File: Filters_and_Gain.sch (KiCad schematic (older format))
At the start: 20 parts, among them U4 OPA388, U5 OPA388, U6 OPA388

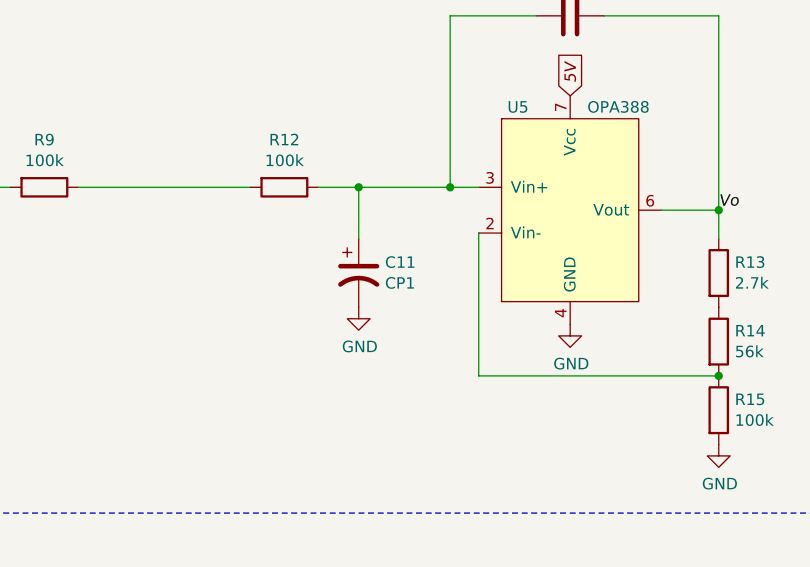
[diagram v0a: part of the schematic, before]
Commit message: Assigned footprints
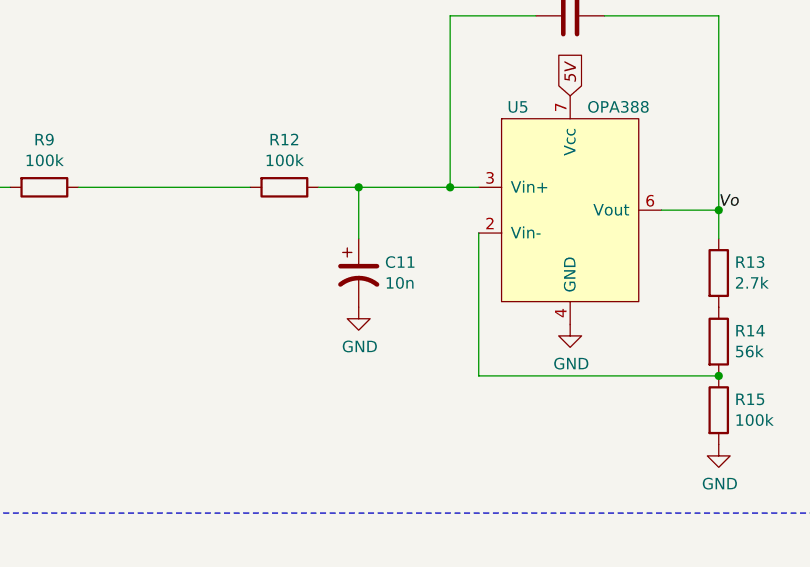
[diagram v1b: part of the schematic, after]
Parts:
- C10, C12, C8, C9: footprint (none) -> Capacitor_SMD:C_0805_2012Metric_Pad1.15x1.40mm_HandSolder
- C11: value CP1 -> 10n; footprint (none) -> Capacitor_SMD:C_0805_2012Metric_Pad1.15x1.40mm_HandSolder
- C13: footprint (none) -> Capacitor_SMD:CP_Elec_6.3x3
- R10, R11, R12, R13, R14, R15, R16, R17, R18, R8, R9: footprint (none) -> Resistor_SMD:R_0805_2012Metric_Pad1.15x1.40mm_HandSolder
- U4, U5, U6: footprint (none) -> Package_SO:SOIC-8_3.9x4.9mm_P1.27mm
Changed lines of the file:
@@
 F 0 "R9" V 2468 2200 50  0000 C CNN
 F 1 "100k" V 2559 2200 50  0000 C CNN
-F 2 "" V 2605 2200 50  0001 C CNN
+F 2 "Resistor_SMD:R_0805_2012Metric_Pad1.15x1.40mm_HandSolder" V 2605 2200 50  0001 C CNN
 F 3 "~" H 2675 2200 50  0001 C CNN
 	1    2675 2200
@@
 F 0 "R12" V 3518 2200 50  0000 C CNN
 F 1 "100k" V 3609 2200 50  0000 C CNN
-F 2 "" V 3655 2200 50  0001 C CNN
+F 2 "Resistor_SMD:R_0805_2012Metric_Pad1.15x1.40mm_HandSolder" V 3655 2200 50  0001 C CNN
 F 3 "~" H 3725 2200 50  0001 C CNN
 	1    3725 2200
@@
 P 4050 2575
 F 0 "C11" H 4165 2621 50  0000 L CNN
-F 1 "CP1" H 4165 2530 50  0000 L CNN
-F 2 "" H 4050 2575 50  0001 C CNN
+F 1 "10n" H 4165 2530 50  0000 L CNN
+F 2 "Capacitor_SMD:C_0805_2012Metric_Pad1.15x1.40mm_HandSolder" H 4050 2575 50  0001 C CNN
 F 3 "~" H 4050 2575 50  0001 C CNN
 	1    4050 2575
@@
 F 0 "U5" H 4700 2750 50  0000 L CNN
 F 1 "OPA388" H 5050 2750 50  0000 L CNN
-F 2 "" H 4975 2300 50  0001 C CNN
-F 3 "" H 4975 2300 50  0001 C CNN
+F 2 "Package_SO:SOIC-8_3.9x4.9mm_P1.27mm" H 4975 2300 50  0001 C CNN
+F 3 "https://www.ti.com/lit/ds/symlink/opa388.pdf" H 4975 2300 50  0001 C CNN
 	1    4975 2300
 	1    0    0    -1
@@
 F 0 "R15" H 5695 3221 50  0000 L CNN
 F 1 "100k" H 5695 3130 50  0000 L CNN
-F 2 "" V 5555 3175 50  0001 C CNN
+F 2 "Resistor_SMD:R_0805_2012Metric_Pad1.15x1.40mm_HandSolder" V 5555 3175 50  0001 C CNN
 F 3 "~" H 5625 3175 50  0001 C CNN
 	1    5625 3175
@@
 F 0 "C12" V 5227 1450 50  0000 C CNN
 F 1 "10n" V 5136 1450 50  0000 C CNN
-F 2 "" H 5013 1300 50  0001 C CNN
+F 2 "Capacitor_SMD:C_0805_2012Metric_Pad1.15x1.40mm_HandSolder" H 5013 1300 50  0001 C CNN
 F 3 "~" H 4975 1450 50  0001 C CNN
 	1    4975 1450
@@
 F 0 "R14" H 5695 2921 50  0000 L CNN
 F 1 "56k" H 5695 2830 50  0000 L CNN
-F 2 "" V 5555 2875 50  0001 C CNN
+F 2 "Resistor_SMD:R_0805_2012Metric_Pad1.15x1.40mm_HandSolder" V 5555 2875 50  0001 C CNN
 F 3 "~" H 5625 2875 50  0001 C CNN
 	1    5625 2875
@@
 F 0 "R13" H 5695 2621 50  0000 L CNN
 F 1 "2.7k" H 5695 2530 50  0000 L CNN
-F 2 "" V 5555 2575 50  0001 C CNN
+F 2 "Resistor_SMD:R_0805_2012Metric_Pad1.15x1.40mm_HandSolder" V 5555 2575 50  0001 C CNN
 F 3 "~" H 5625 2575 50  0001 C CNN
 	1    5625 2575
@@
 F 0 "R8" V 2243 5050 50  0000 C CNN
 F 1 "470k" V 2334 5050 50  0000 C CNN
-F 2 "" V 2380 5050 50  0001 C CNN
+F 2 "Resistor_SMD:R_0805_2012Metric_Pad1.15x1.40mm_HandSolder" V 2380 5050 50  0001 C CNN
 F 3 "~" H 2450 5050 50  0001 C CNN
 	1    2450 5050
@@
 F 0 "R11" V 2993 5050 50  0000 C CNN
 F 1 "470k" V 3084 5050 50  0000 C CNN
-F 2 "" V 3130 5050 50  0001 C CNN
+F 2 "Resistor_SMD:R_0805_2012Metric_Pad1.15x1.40mm_HandSolder" V 3130 5050 50  0001 C CNN
 F 3 "~" H 3200 5050 50  0001 C CNN
 	1    3200 5050
@@
 F 0 "R10" H 2755 5729 50  0000 R CNN
 F 1 "220k" H 2755 5820 50  0000 R CNN
-F 2 "" V 2755 5775 50  0001 C CNN
+F 2 "Resistor_SMD:R_0805_2012Metric_Pad1.15x1.40mm_HandSolder" V 2755 5775 50  0001 C CNN
 F 3 "~" H 2825 5775 50  0001 C CNN
 	1    2825 5775
@@
 F 0 "C8" V 2198 6000 50  0000 C CNN
 F 1 "5n" V 2289 6000 50  0000 C CNN
-F 2 "" H 2488 5850 50  0001 C CNN
+F 2 "Capacitor_SMD:C_0805_2012Metric_Pad1.15x1.40mm_HandSolder" H 2488 5850 50  0001 C CNN
 F 3 "~" H 2450 6000 50  0001 C CNN
 	1    2450 6000
@@
 F 0 "C10" V 2948 6000 50  0000 C CNN
 F 1 "5n" V 3039 6000 50  0000 C CNN
-F 2 "" H 3238 5850 50  0001 C CNN
+F 2 "Capacitor_SMD:C_0805_2012Metric_Pad1.15x1.40mm_HandSolder" H 3238 5850 50  0001 C CNN
 F 3 "~" H 3200 6000 50  0001 C CNN
 	1    3200 6000
@@
 F 0 "C9" H 2710 5179 50  0000 R CNN
 F 1 "10n" H 2710 5270 50  0000 R CNN
-F 2 "" H 2863 5075 50  0001 C CNN
+F 2 "Capacitor_SMD:C_0805_2012Metric_Pad1.15x1.40mm_HandSolder" H 2863 5075 50  0001 C CNN
 F 3 "~" H 2825 5225 50  0001 C CNN
 	1    2825 5225
@@
 F 0 "U4" H 4025 5600 50  0000 L CNN
 F 1 "OPA388" H 4425 5600 50  0000 L CNN
-F 2 "" H 4475 5650 50  0001 C CNN
-F 3 "" H 4475 5650 50  0001 C CNN
+F 2 "Package_SO:SOIC-8_3.9x4.9mm_P1.27mm" H 4475 5650 50  0001 C CNN
+F 3 "https://www.ti.com/lit/ds/symlink/opa388.pdf" H 4475 5650 50  0001 C CNN
 	1    4325 5150
 	1    0    0    -1
@@
 F 0 "C13" V 7177 4600 50  0000 C CNN
 F 1 "100u" V 7086 4600 50  0000 C CNN
-F 2 "" H 6925 4600 50  0001 C CNN
+F 2 "Capacitor_SMD:CP_Elec_6.3x3" H 6925 4600 50  0001 C CNN
 F 3 "~" H 6925 4600 50  0001 C CNN
 	1    6925 4600
@@
 F 0 "R16" H 7370 4496 50  0000 L CNN
 F 1 "3k" H 7370 4405 50  0000 L CNN
-F 2 "" V 7230 4450 50  0001 C CNN
+F 2 "Resistor_SMD:R_0805_2012Metric_Pad1.15x1.40mm_HandSolder" V 7230 4450 50  0001 C CNN
 F 3 "~" H 7300 4450 50  0001 C CNN
 	1    7300 4450
@@
 F 0 "R17" V 7618 4600 50  0000 C CNN
 F 1 "5k" V 7709 4600 50  0000 C CNN
-F 2 "" V 7755 4600 50  0001 C CNN
+F 2 "Resistor_SMD:R_0805_2012Metric_Pad1.15x1.40mm_HandSolder" V 7755 4600 50  0001 C CNN
 F 3 "~" H 7825 4600 50  0001 C CNN
 	1    7825 4600
@@
 F 0 "U6" H 8475 4950 50  0000 L CNN
 F 1 "OPA388" H 8850 4950 50  0000 L CNN
-F 2 "" H 8925 5000 50  0001 C CNN
-F 3 "" H 8925 5000 50  0001 C CNN
+F 2 "Package_SO:SOIC-8_3.9x4.9mm_P1.27mm" H 8925 5000 50  0001 C CNN
+F 3 "https://www.ti.com/lit/ds/symlink/opa388.pdf" H 8925 5000 50  0001 C CNN
 	1    8775 4500
 	1    0    0    -1
@@
 F 0 "R18" V 8675 5400 50  0000 C CNN
 F 1 "100k" V 8875 5400 50  0000 C CNN
-F 2 "" V 8705 5400 50  0001 C CNN
+F 2 "Resistor_SMD:R_0805_2012Metric_Pad1.15x1.40mm_HandSolder" V 8705 5400 50  0001 C CNN
 F 3 "~" H 8775 5400 50  0001 C CNN
 	1    8775 5400

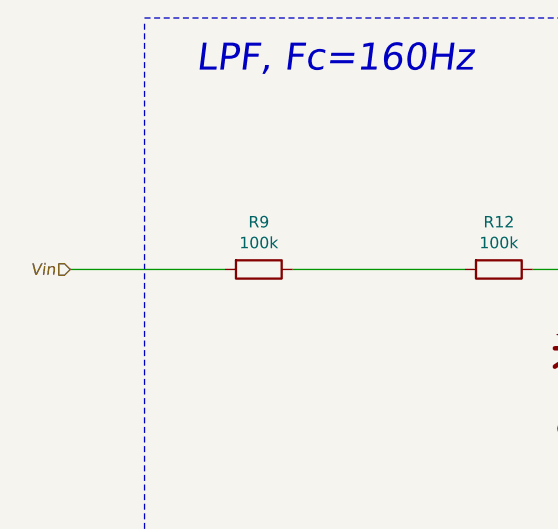
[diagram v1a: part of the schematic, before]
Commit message: #2 - Add ECG input via headphone jack
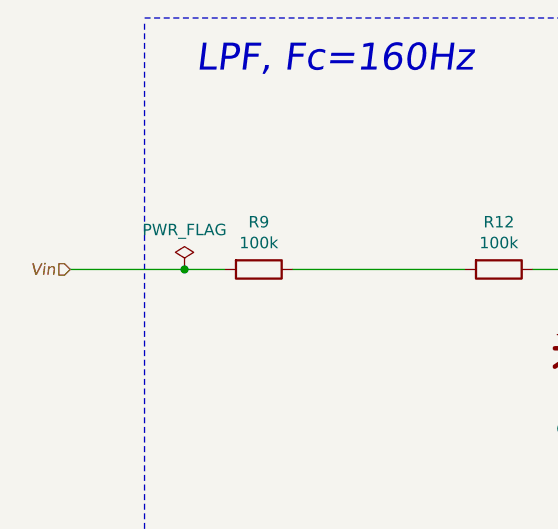
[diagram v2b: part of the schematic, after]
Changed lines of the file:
@@
 Vin
 Wire Wire Line
-	1850 2200 2525 2200
+	1850 2200 2350 2200
 Wire Wire Line
 	9175 4500 9175 5400
+$Comp
+L power:PWR_FLAG #FLG?
+U 1 1 5FBE717F
+P 2350 2200
+F 0 "#FLG?" H 2350 2275 50  0001 C CNN
+F 1 "PWR_FLAG" H 2350 2373 50  0000 C CNN
+F 2 "" H 2350 2200 50  0001 C CNN
+F 3 "~" H 2350 2200 50  0001 C CNN
+	1    2350 2200
+	1    0    0    -1
+$EndComp
+Connection ~ 2350 2200
+Wire Wire Line
+	2350 2200 2525 2200
 $EndSCHEMATC
